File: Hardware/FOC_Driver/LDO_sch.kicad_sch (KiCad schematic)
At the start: 3 parts, among them U3 AP2112K-3.3

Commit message: schematic updates
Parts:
- added C8: 1u, symbol Device:C
- added U4: MA730, Package_DFN_QFN:QFN-16-1EP_3x3mm_P0.5mm_EP1.75x1.75mm, symbol Sensor_Magnetic:MA730
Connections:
- net +3V3: now also C8.1, U4.13 (VDD)
- net GND: now also C8.2, U4.10 (TEST), U4.17 (PAD), U4.8 (GND)
- new net MISO: U4.7 (MISO)
- new net MOSI: U4.4 (MOSI)
- new net SCLK: U4.12 (SCLK)
- new net nCS: U4.5 (~{CS})
- no-connect marks 0 -> 8
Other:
- moved on the sheet: C3, C4, U3

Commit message: Schematic update and Firmware folder
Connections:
- net MISO renamed ENC_MISO
- net MOSI renamed ENC_MOSI
- net SCLK renamed ENC_SCK
- net nCS renamed ENC_CS
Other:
- moved on the sheet: C8, U4

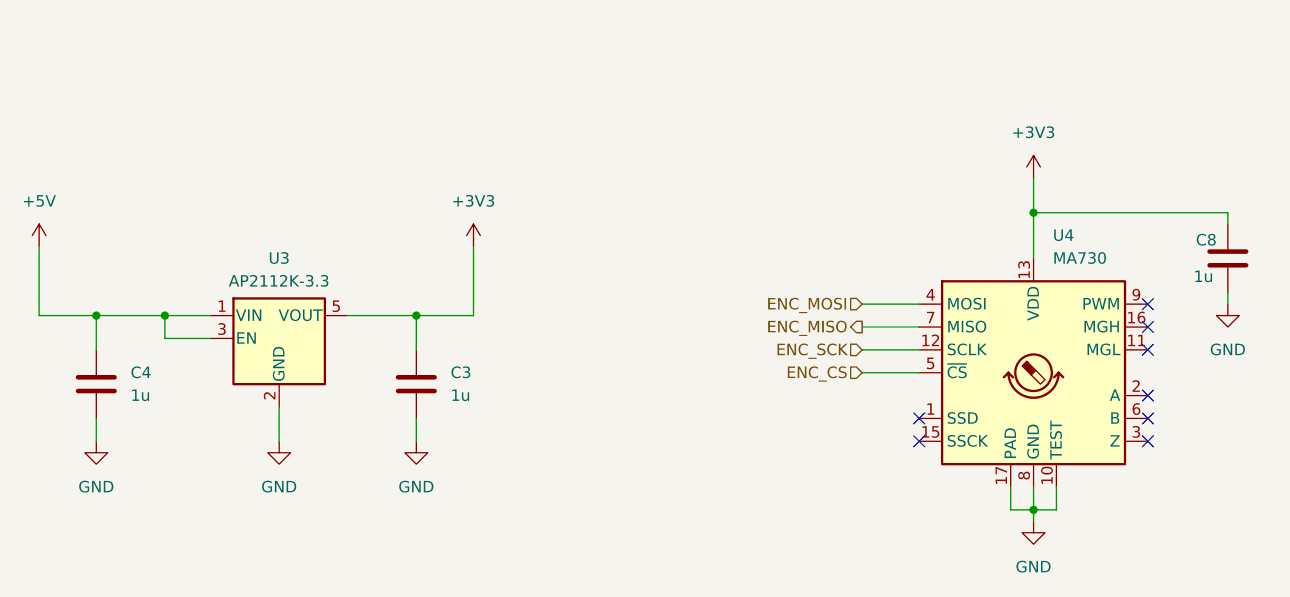
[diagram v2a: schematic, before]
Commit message: schematic completed
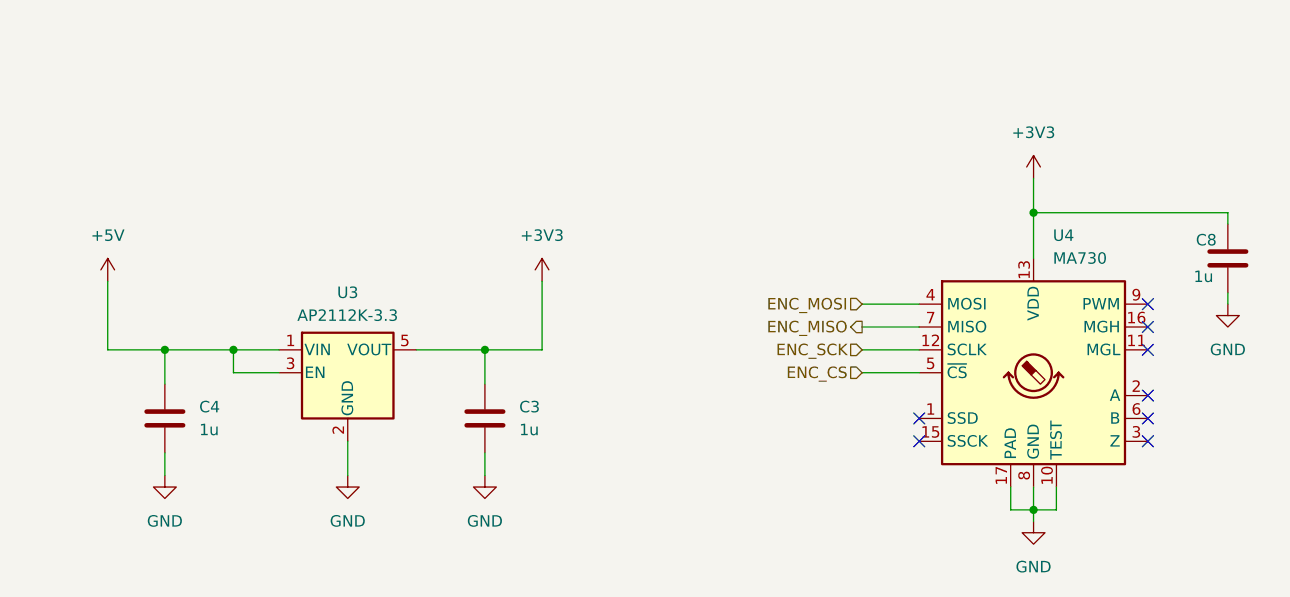
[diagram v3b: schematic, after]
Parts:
- C3, C4, C8: footprint (none) -> eCapacitor:C_0402_1005Metric
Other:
- moved on the sheet: C3, C4, U3
